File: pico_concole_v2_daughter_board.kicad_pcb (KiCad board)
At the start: 2 copper layers, 165.1 x 95.2 mm, 123 parts, among them J1 USB_C_Receptacle_USB2.0_16P, J2 SM03B-SRSS-TB, J3 SM03B-SRSS-TB, J4 Conn_02x12, J5 Conn_02x12, SW1 SW_Push, SW10 SW_Push, SW11 SW_Push, SW12 SW_Push, SW13 SW_Push, SW14 SW_Push, SW15 SW_Push, SW16 SW_Push, SW17 SW_Push, SW2 SW_Push, SW3 SW_Push, SW4 SW_Push, SW5 SW_Push, SW6 SW_Push, SW7 SW_Push, SW8 SW_Push, SW9 SW_Push, U1 RP2350_80QFN, U2 PCM5102A, U3 TSOP34S40F, U4 XPT2046TS, U5 PAM8403D, U6 PAM8403D

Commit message: v2.0.0 WIP
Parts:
- added C1: 100n, Capacitor_SMD:C_0402_1005Metric_Pad0.74x0.62mm_HandSolder, B.Cu at (112.9, 94.5)
- added C10: 100n, Capacitor_SMD:C_0402_1005Metric_Pad0.74x0.62mm_HandSolder, B.Cu at (112.9, 93.5)
- added C11: 100n, Capacitor_SMD:C_0402_1005Metric_Pad0.74x0.62mm_HandSolder, B.Cu at (112.9, 98.4)
- added C12: 100n, Capacitor_SMD:C_0402_1005Metric_Pad0.74x0.62mm_HandSolder, B.Cu at (102.1, 102.1)
- added C13: 4.7u, Capacitor_SMD:C_0603_1608Metric_Pad1.08x0.95mm_HandSolder, B.Cu at (112.6, 102.2)
- added C14: 4.7u, Capacitor_SMD:C_0603_1608Metric_Pad1.08x0.95mm_HandSolder, B.Cu at (110.1, 101.3)
- added C15: 4.7u, Capacitor_SMD:C_0603_1608Metric_Pad1.08x0.95mm_HandSolder, B.Cu at (110.1, 103.0)
- added C16: 100n, Capacitor_SMD:C_0402_1005Metric_Pad0.74x0.62mm_HandSolder, B.Cu at (101.6, 111.8)
- added C17: 15p, Capacitor_SMD:C_0402_1005Metric_Pad0.74x0.62mm_HandSolder, B.Cu at (104.5, 81.9)
- added C18: 15p, Capacitor_SMD:C_0402_1005Metric_Pad0.74x0.62mm_HandSolder, B.Cu at (110.1, 81.9)
- added C19: 1u, Capacitor_SMD:C_0402_1005Metric_Pad0.74x0.62mm_HandSolder, B.Cu at (103.5, 59.7)
- added C2: 100n, Capacitor_SMD:C_0402_1005Metric_Pad0.74x0.62mm_HandSolder, B.Cu at (105.5, 85.9)
- added C20: 1u, Capacitor_SMD:C_0402_1005Metric_Pad0.74x0.62mm_HandSolder, B.Cu at (103.5, 76.1)
- added C3: 100n, Capacitor_SMD:C_0402_1005Metric_Pad0.74x0.62mm_HandSolder, B.Cu at (96.6, 94.1)
- added C4: 100n, Capacitor_SMD:C_0402_1005Metric_Pad0.74x0.62mm_HandSolder, B.Cu at (105.3, 102.1)
- added C5: 100n, Capacitor_SMD:C_0402_1005Metric_Pad0.74x0.62mm_HandSolder, B.Cu at (96.6, 96.6)
- added C6: 100n, Capacitor_SMD:C_0402_1005Metric_Pad0.74x0.62mm_HandSolder, B.Cu at (96.6, 91.7)
- added C7: 100n, Capacitor_SMD:C_0402_1005Metric_Pad0.74x0.62mm_HandSolder, B.Cu at (101.5, 85.9)
- added C8: 100n, Capacitor_SMD:C_0402_1005Metric_Pad0.74x0.62mm_HandSolder, B.Cu at (103.9, 85.9)
- added C9: 100n, Capacitor_SMD:C_0402_1005Metric_Pad0.74x0.62mm_HandSolder, B.Cu at (112.9, 89.3)
- added R11: 1k, Resistor_SMD:R_0402_1005Metric_Pad0.72x0.64mm_HandSolder, B.Cu at (119.4, 49.5)
- added R16: 330k, Resistor_SMD:R_0402_1005Metric_Pad0.72x0.64mm_HandSolder, B.Cu at (141.6, 151.8)
- added R17: 330k, Resistor_SMD:R_0402_1005Metric_Pad0.72x0.64mm_HandSolder, B.Cu at (69.2, 83.8)
- added R18: 1k, Resistor_SMD:R_0402_1005Metric_Pad0.72x0.64mm_HandSolder, B.Cu at (148.0, 151.8)
- added R19: 1k, Resistor_SMD:R_0402_1005Metric_Pad0.72x0.64mm_HandSolder, B.Cu at (69.2, 86.8)
- added R3: 33, Resistor_SMD:R_0603_1608Metric_Pad0.98x0.95mm_HandSolder, B.Cu at (114.3, 102.2)
- added R4: 27, Resistor_SMD:R_0402_1005Metric_Pad0.72x0.64mm_HandSolder, B.Cu at (106.3, 102.1)
- added R5: 27, Resistor_SMD:R_0402_1005Metric_Pad0.72x0.64mm_HandSolder, B.Cu at (107.3, 102.1)
- added R6: 1k, Resistor_SMD:R_0402_1005Metric_Pad0.72x0.64mm_HandSolder, B.Cu at (95.9, 111.1)
- added R7: 1k, Resistor_SMD:R_0402_1005Metric_Pad0.72x0.64mm_HandSolder, B.Cu at (115.6, 112.4)
- added R8: 1k, Resistor_SMD:R_0402_1005Metric_Pad0.72x0.64mm_HandSolder, B.Cu at (107.3, 84.3)
- added SW1: SW_Push, Button_Switch_SMD:SW_Push_1P1T_NO_Vertical_Wuerth_434133025816, F.Cu at (99.7, 109.2)
- added SW2: SW_Push, Button_Switch_SMD:SW_Push_1P1T_NO_Vertical_Wuerth_434133025816, F.Cu at (116.2, 109.2)
- added TP1: TP, TestPoint:TestPoint_Pad_1.0x1.0mm, B.Cu at (63.5, 39.9)
- added TP25: TP, TestPoint:TestPoint_Pad_1.0x1.0mm, B.Cu at (110.4, 62.2)
- added TP26: TP, TestPoint:TestPoint_Pad_1.0x1.0mm, B.Cu at (110.4, 65.3)
- added TP27: TP, TestPoint:TestPoint_Pad_1.0x1.0mm, B.Cu at (107.3, 62.2)
- added TP28: TP, TestPoint:TestPoint_Pad_1.0x1.0mm, B.Cu at (107.3, 65.3)
- added TP29: TP, TestPoint:TestPoint_Pad_1.0x1.0mm, B.Cu at (104.3, 62.2)
- added TP30: TP, TestPoint:TestPoint_Pad_1.0x1.0mm, B.Cu at (104.3, 65.3)
- added U2: W25Q16JVSS, Package_SO:SOIC-8_5.3x5.3mm_P1.27mm, B.Cu at (98.4, 107.3)
- added Y1: ABM8-272-T3, Crystal:Crystal_SMD_3225-4Pin_3.2x2.5mm, B.Cu at (107.3, 81.9)
- R10: renamed from R7; footprint Resistor_SMD:R_0805_2012Metric_Pad1.20x1.40mm_HandSolder -> Resistor_SMD:R_0402_1005Metric_Pad0.72x0.64mm_HandSolder
- R12: renamed from R9; footprint Resistor_SMD:R_0603_1608Metric_Pad0.98x0.95mm_HandSolder -> Resistor_SMD:R_0402_1005Metric_Pad0.72x0.64mm_HandSolder
- R13: renamed from R10; footprint Resistor_SMD:R_0603_1608Metric_Pad0.98x0.95mm_HandSolder -> Resistor_SMD:R_0402_1005Metric_Pad0.72x0.64mm_HandSolder
- R14: renamed from R11; footprint Resistor_SMD:R_0603_1608Metric_Pad0.98x0.95mm_HandSolder -> Resistor_SMD:R_0402_1005Metric_Pad0.72x0.64mm_HandSolder
- R15: renamed from R12; footprint Resistor_SMD:R_0603_1608Metric_Pad0.98x0.95mm_HandSolder -> Resistor_SMD:R_0402_1005Metric_Pad0.72x0.64mm_HandSolder
- R9: renamed from R8; footprint Resistor_SMD:R_0805_2012Metric_Pad1.20x1.40mm_HandSolder -> Resistor_SMD:R_0402_1005Metric_Pad0.72x0.64mm_HandSolder
- moved TP16 141.7 mm to (74.3, -15.9)
- moved TP18 141.7 mm to (74.3, -13.3)
- moved TP20 141.7 mm to (74.3, -10.8)
- moved TP22 141.7 mm to (74.3, -8.26)
- moved JP1 141.1 mm to (77.5, -15.9)
- moved JP2 141.1 mm to (77.5, -13.3)
- moved JP3 141.1 mm to (77.5, -10.8)
- moved JP4 141.1 mm to (77.5, -8.26)
- moved TP15 140.5 mm to (80.6, -15.9)
- moved TP17 140.5 mm to (80.6, -13.3)
- moved TP19 140.5 mm to (80.6, -10.8)
- moved TP21 140.5 mm to (80.6, -8.26)
- moved R20 140.2 mm to (70.7, -15.7)
- moved R21 140.2 mm to (70.7, -13.2)
- moved R22 140.2 mm to (70.7, -10.7)
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- renumbered C1 to C21, C8 to C22, C2 to C23, C9 to C24, C3 to C25, C10 to C26, C4 to C27, C5 to C28, C6 to C29, C7 to C30, C11 to C31, C12 to C32, C13 to C33, C14 to C34, D7 to D10, D15 to D12, D4 to D13, D8 to D14, D12 to D15, D5 to D2, D9 to D3, D13 to D4, D2 to D5, D10 to D7, D14 to D8, D3 to D9, H11 to H10, H6 to H11, H7 to H2, H2 to H3, H8 to H4, H3 to H5, H9 to H6, H4 to H7, H10 to H8, H5 to H9, J2 to J1, J3 to J2, J1 to J3, LED5 to LED1, LED1 to LED2, LED2 to LED3, LED3 to LED4, LED4 to LED5, R3 to R20, R4 to R21, R5 to R22, R6 to R23, SW11 to SW10, SW15 to SW11, SW4 to SW12, SW8 to SW13, SW12 to SW14, SW16 to SW15, SW5 to SW16, SW9 to SW17, SW13 to SW18, SW17 to SW19, SW1 to SW3, SW2 to SW4, SW6 to SW5, SW10 to SW6, SW14 to SW7, SW3 to SW8, SW7 to SW9, TP15 to TP10, TP16 to TP11, TP17 to TP12, TP18 to TP13, TP23 to TP14, TP2 to TP15, TP6 to TP16, TP3 to TP17, TP7 to TP18, TP4 to TP19, TP21 to TP2, TP8 to TP20, TP5 to TP21, TP9 to TP22, TP1 to TP23, TP10 to TP24, TP22 to TP3, TP19 to TP4, TP20 to TP5, TP11 to TP6, TP12 to TP7, TP13 to TP8, TP14 to TP9, U2 to U5, U5 to U6, U6 to U7
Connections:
- C21 pad 1: /Daughterboard/SPK_R -> Net-(C21-Pad1)
- C22 pad 1: /Daughterboard/GPIO8 -> Net-(C22-Pad1)
- C23 pad 1: /Daughterboard/GPIO10 -> Net-(C23-Pad1)
- C24 pad 1: /Daughterboard/SPK_L -> Net-(C24-Pad1)
- J4 pad 7: /Main/MAIN_GPIO09 -> /Daughterboard/MAIN_GPIO9
- U1 pad 10: unconnected-(U1-DVDD-Pad10) -> +1V1
- U1 pad 15: unconnected-(U1-IOVDD-Pad15) -> +3V3
- U1 pad 24: unconnected-(U1-IOVDD-Pad24) -> +3V3
- U1 pad 29: unconnected-(U1-IOVDD-Pad29) -> +3V3
- U1 pad 32: unconnected-(U1-DVDD-Pad32) -> +1V1
- U1 pad 35: /Southbridge/RUN -> /Daughterboard/~{SB_RUN}
- U1 pad 41: unconnected-(U1-IOVDD-Pad41) -> +3V3
- U1 pad 5: unconnected-(U1-IOVDD-Pad5) -> +3V3
- U1 pad 50: unconnected-(U1-IOVDD-Pad50) -> +3V3
- U1 pad 51: unconnected-(U1-DVDD-Pad51) -> +1V1
- U1 pad 59: unconnected-(U1-ADC_AVDD-Pad59) -> +3V3
- U1 pad 60: unconnected-(U1-IOVDD-Pad60) -> +3V3
- U1 pad 61: unconnected-(U1-VREG_AVDD-Pad61) -> /Southbridge/VREG_AVDD
- U1 pad 62: unconnected-(U1-VREG_PGND-Pad62) -> GND
- U1 pad 63: unconnected-(U1-VREG_LX-Pad63) -> /Southbridge/VREG_LX
- U1 pad 64: unconnected-(U1-VREG_VIN-Pad64) -> +3V3
- U1 pad 65: unconnected-(U1-VREG_FB-Pad65) -> +1V1
- U1 pad 66: unconnected-(U1-USB_DM-Pad66) -> /Southbridge/RP2350_D-
- U1 pad 67: unconnected-(U1-USB_DP-Pad67) -> /Southbridge/RP2350_D+
- U1 pad 68: unconnected-(U1-USB_OTP_VDD-Pad68) -> +3V3
- U1 pad 69: unconnected-(U1-QSPI_IOVDD-Pad69) -> +3V3
- U1 pad 76: unconnected-(U1-IOVDD-Pad76) -> +3V3
- U1 pad 81: unconnected-(U1-GND-Pad81) -> GND
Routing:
- net (no net): track 359.3 -> 860.6 mm
- net /Daughterboard/GPIO27: track 0.00 -> 433.5 mm, vias 1 -> 2
- net /Daughterboard/~{MAIN_RUN}: track 4.15 -> 133.6 mm, vias 0 -> 3
- net /Daughterboard/GPIO3: track 0.00 -> 93.4 mm, vias 0 -> 4
- net /Daughterboard/MAIN_GPIO12: track 0.00 -> 82.4 mm, vias 0 -> 5
- net /Daughterboard/MAIN_GPIO13: track 0.00 -> 82.2 mm, vias 0 -> 5
- net /Daughterboard/GPIO2: track 0.00 -> 81.6 mm, vias 0 -> 3
- net /Daughterboard/GPIO43: track 27.9 -> 107.6 mm
- net /Daughterboard/~{SB_RUN}: track 0.00 -> 76.8 mm, vias 0 -> 1
- net /Daughterboard/GPIO42: track 32.2 -> 108.3 mm
- net /Daughterboard/MAIN_GPIO19: track 0.00 -> 58.9 mm, vias 0 -> 2
- net +3V3: track 0.00 -> 51.8 mm, vias 0 -> 5
- net /Daughterboard/MAIN_GPIO18: track 0.00 -> 49.4 mm, vias 0 -> 2
- net /Daughterboard/GPIO39: track 0.00 -> 46.6 mm, vias 0 -> 1
- net /Daughterboard/MAIN_GPIO15: track 0.00 -> 44.4 mm, vias 0 -> 2
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- added copper zone on B.Cu, net +1V1
- added copper zone on B.Cu, net +3V3
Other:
- board text added: "1"
- board text added: "2"
- board text added: "3"
- board text added: "3.5 Jack"
- board text added: "4"
- board text added: "BOOT(SB)"
- board text added: "GPIO09"
- board text added: "GPIO10"
- board text added: "GPIO11"
- board text added: "GPIO47"
- board text added: "MAIN"
- board text added: "RUN(SB)"

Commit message: v2.0.0 WIP
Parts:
- added L1: AOTA-B201610S3R3-101-T, Library:L_pol_2016, B.Cu at (110.7, 104.8)
- R3: footprint Resistor_SMD:R_0603_1608Metric_Pad0.98x0.95mm_HandSolder -> Capacitor_SMD:C_0402_1005Metric_Pad0.74x0.62mm_HandSolder
- U1: footprint Library:QFN-80-1EP_10x10mm_P0.4mm_EP3.4x3.4mm_ThermalVias -> Package_DFN_QFN:QFN-80-1EP_10x10mm_P0.4mm_EP3.4x3.4mm
- moved D13 127.0 mm to (59.4, 16.5)
- moved D14 120.9 mm to (158.4, 17.8)
- moved D15 67.2 mm to (53.3, 118.7)
- moved C21 59.9 mm to (144.8, 94.6)
- moved C23 59.9 mm to (153.7, 94.6)
- moved C27 59.9 mm to (144.1, 96.5)
- moved C30 59.9 mm to (154.3, 96.5)
- moved U6 59.9 mm to (149.2, 98.4)
- moved C25 59.9 mm to (149.2, 92.6)
- moved C28 59.9 mm to (154.3, 99.1)
- moved C29 59.9 mm to (144.1, 99.1)
- moved R12 59.9 mm to (144.1, 97.8)
- moved R13 59.9 mm to (154.3, 97.8)
- moved R18 59.3 mm to (153.0, 92.7), turned to 0 degrees
- moved LRA2 58.7 mm to (165.7, 101.0)
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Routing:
- net (no net): track 860.6 -> 1387.9 mm
- net /Daughterboard/GPIO27: track 433.5 -> 27.1 mm
- net /Daughterboard/SPK_L: track 0.00 -> 75.2 mm, vias 0 -> 2
- net /Daughterboard/GPIO42: track 108.3 -> 33.8 mm
- net /Daughterboard/GPIO43: track 107.6 -> 33.2 mm
- net GNDA: track 0.00 -> 67.7 mm, vias 6 -> 16
- net VBUS: track 7.23 -> 51.4 mm, vias 0 -> 2
- net VIN: track 5.05 -> 47.8 mm, vias 0 -> 1
- net +3V3: track 51.8 -> 86.7 mm
- net /Daughterboard/MAIN_GPIO25: track 4.48 -> 35.1 mm
- net /Daughterboard/~{SB_RUN}: track 76.8 -> 48.3 mm
- net /Daughterboard/SPK_R: track 0.00 -> 25.1 mm
- net /Daughterboard/AMP_L: track 0.00 -> 21.5 mm, vias 0 -> 2
- net /Daughterboard/AMP_R: track 0.00 -> 19.2 mm, vias 0 -> 2
- net /Daughterboard/SPK_R+: track 0.00 -> 17.1 mm, vias 0 -> 2
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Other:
- board text added: "CS"
- board text added: "DC"
- board text added: "GPIO06"
- board text added: "GPIO07"
- board text added: "GPIO12"
- board text added: "GPIO13"
- board text added: "GPIO14"
- board text added: "GPIO15"
- board text added: "GPIO16"
- board text added: "GPIO17"
- board text added: "GPIO18"
- board text added: "GPIO19"
- board text added: "MISO"
- board text added: "MOSI"
- board text added: "RST"
- board text added: "SCK"

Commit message: V2.0.0 WIP
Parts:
- removed the TP10 at (78.7, 90.4)
- removed the TP12 at (78.7, 88.3)
- removed the TP13 at (80.8, 87.1)
- removed the TP6 at (78.7, 94.7)
- removed the TP7 at (80.8, 93.6)
- removed the TP8 at (78.7, 92.6)
- added J6: Conn_01x10_MountingPin, Connector_FFC-FPC:TE_1-1734839-0_1x10-1MP_P0.5mm_Horizontal, B.Cu at (81.3, 90.2)
- added TP14: TP, TestPoint:TestPoint_Pad_D1.0mm, B.Cu at (106.4, 68.3)
- added TP16: TP, TestPoint:TestPoint_Pad_D1.0mm, B.Cu at (37.3, 71.0)
- added TP17: TP, TestPoint:TestPoint_Pad_D1.0mm, B.Cu at (39.4, 71.0)
- added TP18: TP, TestPoint:TestPoint_Pad_D1.0mm, B.Cu at (41.4, 71.0)
- added TP25: TP, TestPoint:TestPoint_Pad_D1.0mm, B.Cu at (182.4, 70.0)
- added TP26: TP, TestPoint:TestPoint_Pad_D1.0mm, B.Cu at (180.3, 70.0)
- added TP27: TP, TestPoint:TestPoint_Pad_D1.0mm, B.Cu at (178.3, 70.0)
- added U1: USBLC6-2SC6, Package_TO_SOT_SMD:SOT-23-6, B.Cu at (107.7, 107.3)
- SW3: footprint Button_Switch_SMD:SW_SPST_PTS810 -> Button_Switch_SMD:SW_Push_1P1T_NO_Vertical_Wuerth_434133025816
- TP1, TP11, TP2, TP3, TP4, TP9: footprint TestPoint:TestPoint_Pad_1.0x1.0mm -> TestPoint:TestPoint_Pad_D1.0mm
- TP10: renamed from TP27; footprint TestPoint:TestPoint_Pad_1.0x1.0mm -> TestPoint:TestPoint_Pad_D1.0mm
- TP12: renamed from TP26; footprint TestPoint:TestPoint_Pad_1.0x1.0mm -> TestPoint:TestPoint_Pad_D1.0mm
- TP13: renamed from TP25; footprint TestPoint:TestPoint_Pad_1.0x1.0mm -> TestPoint:TestPoint_Pad_D1.0mm
- TP15: renamed from TP14; footprint TestPoint:TestPoint_Pad_1.0x1.0mm -> TestPoint:TestPoint_Pad_D1.0mm
- TP19: renamed from TP15; footprint TestPoint:TestPoint_Pad_1.5x1.5mm -> TestPoint:TestPoint_Pad_1.0x1.0mm
- TP20: renamed from TP16; footprint TestPoint:TestPoint_Pad_1.5x1.5mm -> TestPoint:TestPoint_Pad_1.0x1.0mm
- TP21: renamed from TP17; footprint TestPoint:TestPoint_Pad_1.5x1.5mm -> TestPoint:TestPoint_Pad_1.0x1.0mm
- TP22: renamed from TP18; footprint TestPoint:TestPoint_Pad_1.5x1.5mm -> TestPoint:TestPoint_Pad_1.0x1.0mm
- TP23: renamed from TP19; footprint TestPoint:TestPoint_Pad_1.5x1.5mm -> TestPoint:TestPoint_Pad_1.0x1.0mm
- TP24: renamed from TP20; footprint TestPoint:TestPoint_Pad_1.5x1.5mm -> TestPoint:TestPoint_Pad_1.0x1.0mm
- TP28: renamed from TP21; footprint TestPoint:TestPoint_Pad_1.5x1.5mm -> TestPoint:TestPoint_Pad_1.0x1.0mm
- TP29: renamed from TP22; footprint TestPoint:TestPoint_Pad_1.5x1.5mm -> TestPoint:TestPoint_Pad_1.0x1.0mm
- TP30: renamed from TP23; footprint TestPoint:TestPoint_Pad_1.5x1.5mm -> TestPoint:TestPoint_Pad_1.0x1.0mm
- TP31: renamed from TP24; footprint TestPoint:TestPoint_Pad_1.5x1.5mm -> TestPoint:TestPoint_Pad_1.0x1.0mm
- TP5: renamed from TP30; footprint TestPoint:TestPoint_Pad_1.0x1.0mm -> TestPoint:TestPoint_Pad_D1.0mm
- TP6: renamed from TP5; footprint TestPoint:TestPoint_Pad_1.0x1.0mm -> TestPoint:TestPoint_Pad_D1.0mm
- TP7: renamed from TP29; footprint TestPoint:TestPoint_Pad_1.0x1.0mm -> TestPoint:TestPoint_Pad_D1.0mm
- TP8: renamed from TP28; footprint TestPoint:TestPoint_Pad_1.0x1.0mm -> TestPoint:TestPoint_Pad_D1.0mm
- moved R20 70.0 mm to (104.1, 45.7)
- moved JP1 69.9 mm to (110.5, 45.7)
- moved TP19 69.9 mm to (113.7, 45.7), turned to 0 degrees
- moved TP20 69.9 mm to (107.3, 45.7), turned to 0 degrees
- moved R21 65.5 mm to (104.1, 43.2)
- moved JP2 65.5 mm to (110.5, 43.2)
- moved TP21 65.5 mm to (113.7, 43.2), turned to 0 degrees
- moved TP22 65.5 mm to (107.3, 43.2), turned to 0 degrees
- moved R22 61.2 mm to (104.1, 40.6)
- moved JP3 61.1 mm to (110.5, 40.6)
- moved TP23 61.1 mm to (113.7, 40.6), turned to 0 degrees
- moved TP24 61.1 mm to (107.3, 40.6), turned to 0 degrees
- moved R23 57.0 mm to (104.1, 38.1)
- moved JP4 56.9 mm to (110.5, 38.1)
- moved TP28 56.9 mm to (113.7, 38.1), turned to 0 degrees
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- renumbered C22 to C21, C21 to C22, C24 to C23, C23 to C24, C26 to C25, C25 to C26, C31 to C27, C32 to C28, C33 to C29, C34 to C30, C27 to C31, C28 to C32, C29 to C33, C30 to C34, R14 to R12, R15 to R13, R12 to R14, R13 to R15, R17 to R16, R16 to R17, R19 to R18, R18 to R19, U1 to U2, U2 to U3, U3 to U4, U4 to U5, U5 to U6, U6 to U8
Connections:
- net Net-(DP1-Pin_5) renamed /Daughterboard/DP_LED_K
- AUDIO1 pad S: GNDA -> GND
- C25 pad 2: GNDA -> GND
- C26 pad 2: GNDA -> GND
- C27 pad 1: VIN -> +3V3
- C27 pad 2: GNDA -> GND
- C28 pad 1: VIN -> +3V3
- C28 pad 2: GNDA -> GND
- C29 pad 1: VIN -> +3V3
- C29 pad 2: GNDA -> GND
- C30 pad 1: VIN -> +3V3
- C30 pad 2: GNDA -> GND
- C31 pad 1: VIN -> +3V3
- C31 pad 2: GNDA -> GND
- C32 pad 1: VIN -> +3V3
- C32 pad 2: GNDA -> GND
- C33 pad 1: VIN -> +3V3
- C33 pad 2: GNDA -> GND
- C34 pad 1: VIN -> +3V3
- C34 pad 2: GNDA -> GND
- DP1 pad 8: unconnected-(DP1-Pin_8-Pad8) -> /Daughterboard/DP_LED_A
- J3 pad A4: VBUS -> VUSB
- J3 pad A9: VBUS -> VUSB
- J3 pad B4: VBUS -> VUSB
- J3 pad B9: VBUS -> VUSB
- R12 pad 1: VIN -> +3V3
- R13 pad 1: VIN -> +3V3
- R14 pad 1: VIN -> +3V3
- R15 pad 1: VIN -> +3V3
- R19 pad 1: /Daughterboard/GPIO10 -> /Daughterboard/GPIO9
- TP11 pad 1: /Daughterboard/GPIO17 -> /Daughterboard/GPIO11
- TP30 pad 1: VIN -> +3V3
- TP9 pad 1: /Daughterboard/GPIO15 -> /Daughterboard/GPIO10
- U6 pad 1: unconnected-(U5-CPVDD-Pad1) -> +3V3
- U6 pad 19: unconnected-(U5-DGND-Pad19) -> GND
- U6 pad 3: unconnected-(U5-CPGND-Pad3) -> GND
- U6 pad 8: unconnected-(U5-AVDD-Pad8) -> +3V3
- U6 pad 9: unconnected-(U5-AGND-Pad9) -> GND
- U7 pad 11: GNDA -> GND
- U7 pad 13: VIN -> +3V3
- U7 pad 15: GNDA -> GND
- U7 pad 2: GNDA -> GND
- U7 pad 4: VIN -> +3V3
- U7 pad 6: VIN -> +3V3
- U8 pad 11: GNDA -> GND
- U8 pad 13: VIN -> +3V3
- U8 pad 15: GNDA -> GND
- U8 pad 2: GNDA -> GND
- U8 pad 4: VIN -> +3V3
- U8 pad 6: VIN -> +3V3
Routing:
- net +3V3: track 86.7 -> 405.5 mm, vias 5 -> 25
- net GND: track 10.7 -> 154.8 mm, vias 91 -> 191
- net (no net): track 1387.9 -> 1262.3 mm
- net /Daughterboard/GPIO27: track 27.1 -> 152.7 mm, vias 2 -> 4
- net VUSB: track 14.9 -> 139.8 mm, vias 1 -> 4
- net /Daughterboard/GPIO41: track 48.6 -> 132.9 mm, vias 2 -> 4
- net /Daughterboard/GPIO43: track 33.2 -> 115.2 mm, vias 1 -> 2
- net /Daughterboard/GPIO42: track 33.8 -> 114.6 mm, vias 1 -> 2
- net /Daughterboard/GPIO26: track 21.0 -> 101.4 mm, vias 1 -> 2
- net /Daughterboard/GPIO40: track 46.7 -> 126.8 mm, vias 2 -> 4
- net GNDA: track 67.7 -> 0.00 mm, vias 16 -> 0
- net /Daughterboard/GPIO9: track 9.49 -> 71.2 mm, vias 1 -> 4
- net VBUS: track 51.4 -> 0.00 mm, vias 2 -> 0
- net /Daughterboard/GPIO44: track 4.07 -> 47.7 mm
- net VIN: track 47.8 -> 5.05 mm, vias 1 -> 0
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- added copper zone on B.Cu, net /Daughterboard/DP_LED_K
- added copper zone on B.Cu, net /Southbridge/VREG_LX
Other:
- board text added: "3V3"
- board text added: "40"
- board text added: "BL"
- board text added: "For WL module"
- board text added: "GND"
- board text added: "HSTX 3V3 GND"
- board text added: "SELECT (-)"
- board text added: "START (+)"
- board text removed: "GPIO12"
- board text removed: "GPIO13"
- board text removed: "GPIO14"
- board text removed: "GPIO15"
- board text removed: "GPIO16"
- board text removed: "GPIO17"
- board text removed: "GPIO18"
- board text removed: "GPIO19"
- board text removed: "SELECT"
- board text removed: "START"

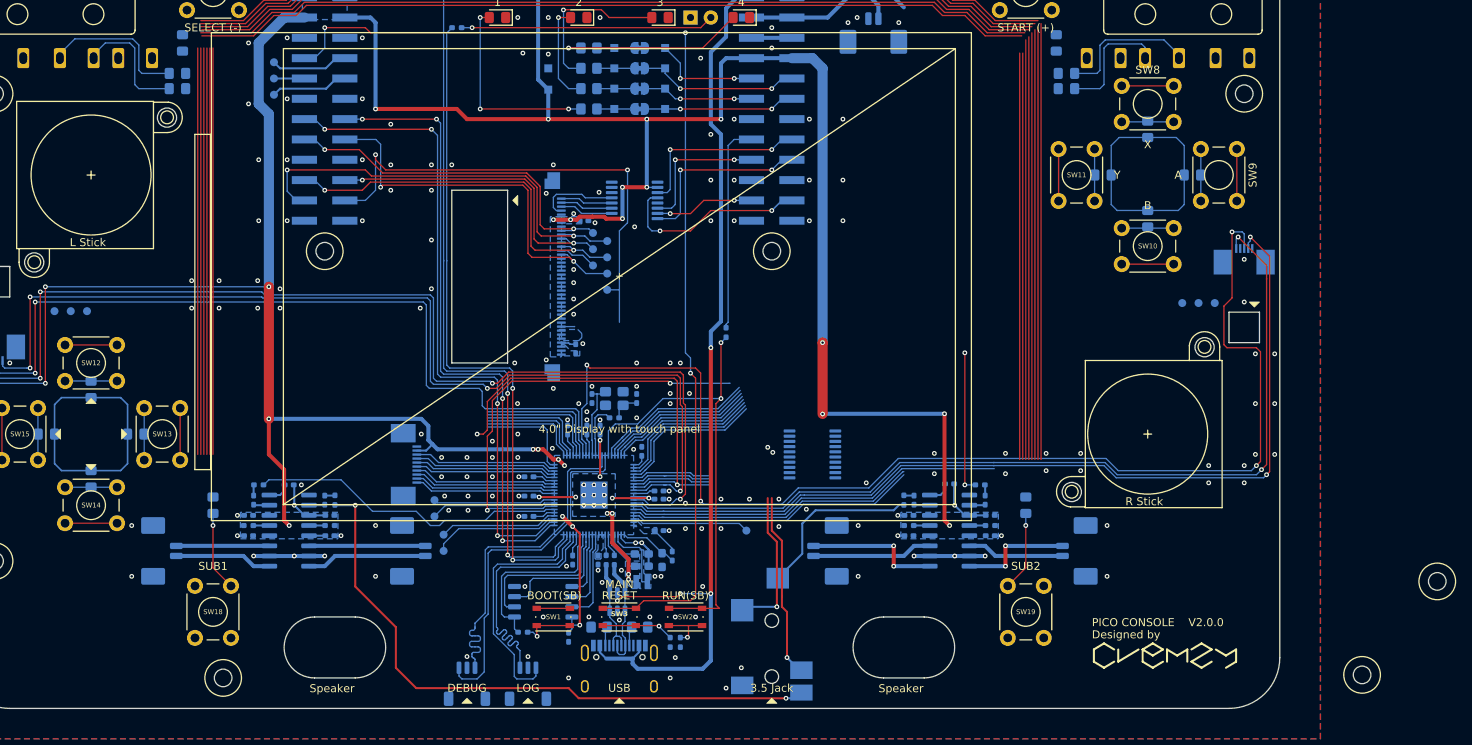
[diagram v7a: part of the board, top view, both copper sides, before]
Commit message: Update LCD pin assignments
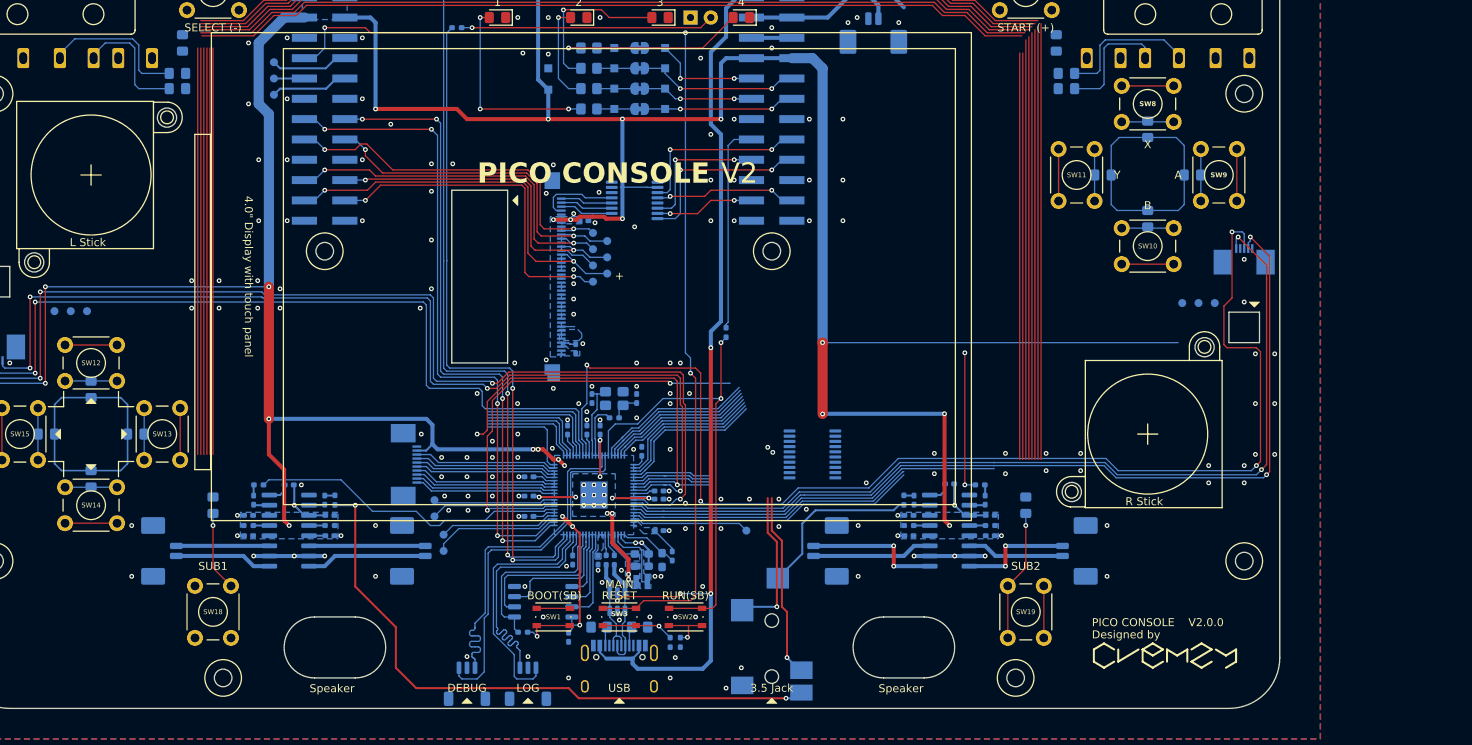
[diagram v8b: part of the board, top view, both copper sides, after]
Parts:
- R16, R17: value 330k -> 100k
- moved H4 43.3 mm to (157.5, 116.8)
- moved H6 24.3 mm to (186.1, 102.2)
- moved TP14 2.05 mm to (104.6, 67.3)
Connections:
- DP1 pad 26: /Daughterboard/MAIN_GPIO15 -> /Daughterboard/MAIN_GPIO18
- DP1 pad 28: /Daughterboard/MAIN_GPIO16 -> /Daughterboard/MAIN_GPIO17
- DP1 pad 30: /Daughterboard/MAIN_GPIO17 -> /Daughterboard/MAIN_GPIO16
- DP1 pad 31: /Daughterboard/MAIN_GPIO18 -> /Daughterboard/MAIN_GPIO15
- TP10 pad 1: /Daughterboard/MAIN_GPIO16 -> /Daughterboard/MAIN_GPIO17
- TP13 pad 1: /Daughterboard/MAIN_GPIO15 -> /Daughterboard/MAIN_GPIO18
- TP7 pad 1: /Daughterboard/MAIN_GPIO18 -> /Daughterboard/MAIN_GPIO15
- TP8 pad 1: /Daughterboard/MAIN_GPIO17 -> /Daughterboard/MAIN_GPIO16
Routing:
- net +3V3: track 405.5 -> 450.4 mm, vias 25 -> 23
- net /Daughterboard/MAIN_GPIO19: track 62.5 -> 43.0 mm
- net /Daughterboard/MAIN_GPIO20: track 24.4 -> 17.7 mm
- net /Daughterboard/GPIO31: track 31.6 -> 38.1 mm
- net Net-(D16-A): track 9.99 -> 16.5 mm
- net /Daughterboard/MAIN_GPIO15: track 49.6 -> 43.7 mm
- net /Daughterboard/MAIN_GPIO17: track 40.2 -> 43.0 mm
- net /Daughterboard/MAIN_GPIO18: track 53.9 -> 51.3 mm
- net /Daughterboard/MAIN_GPIO16: track 48.6 -> 46.5 mm
- net /Daughterboard/MAIN_GPIO14: track 45.4 -> 46.2 mm
- net /Daughterboard/~{SB_RUN}: track 59.7 -> 58.8 mm
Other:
- board text added: "LCD"
- board text added: "V2"
- board text added: "WL module & LED"
- board text removed: "For WL module"
